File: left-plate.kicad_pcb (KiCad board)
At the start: 2 copper layers, 154.5 x 96.2 mm, 26 parts

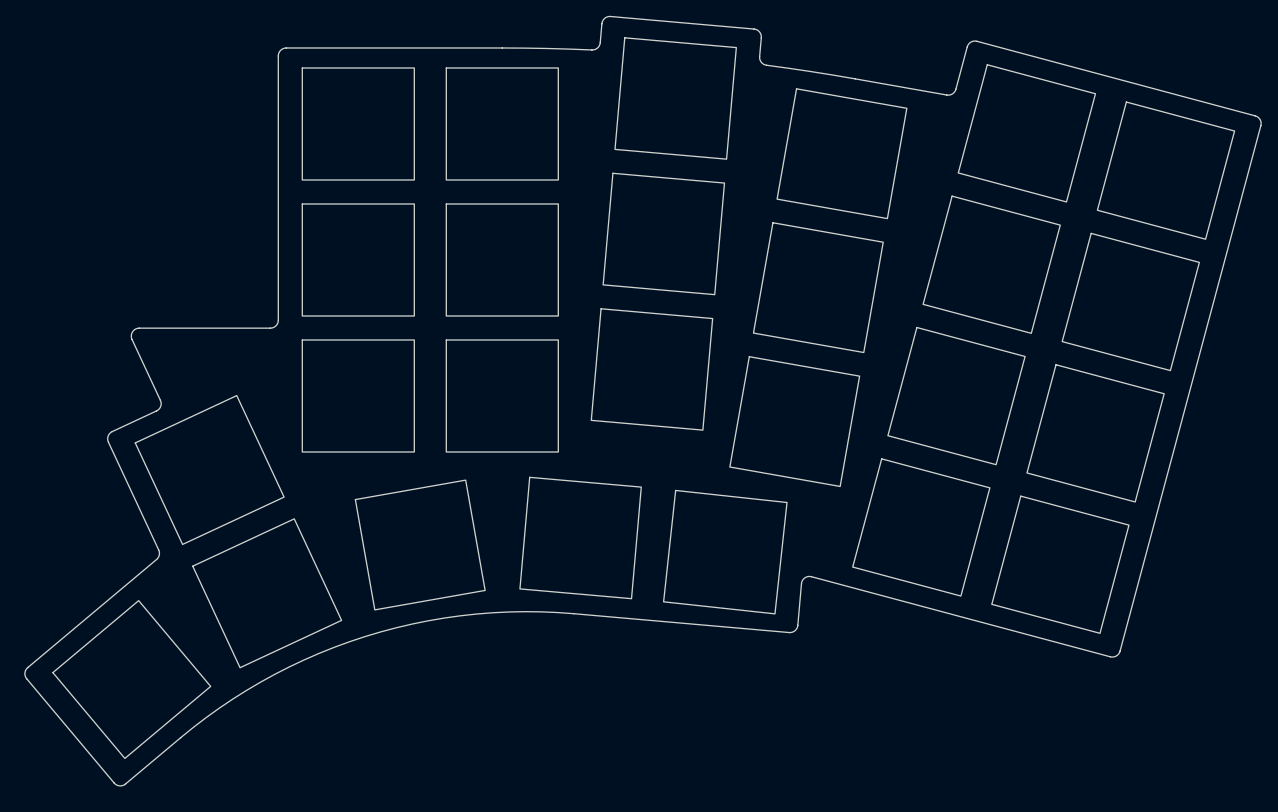
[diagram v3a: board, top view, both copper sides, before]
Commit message: remove two thumb keys
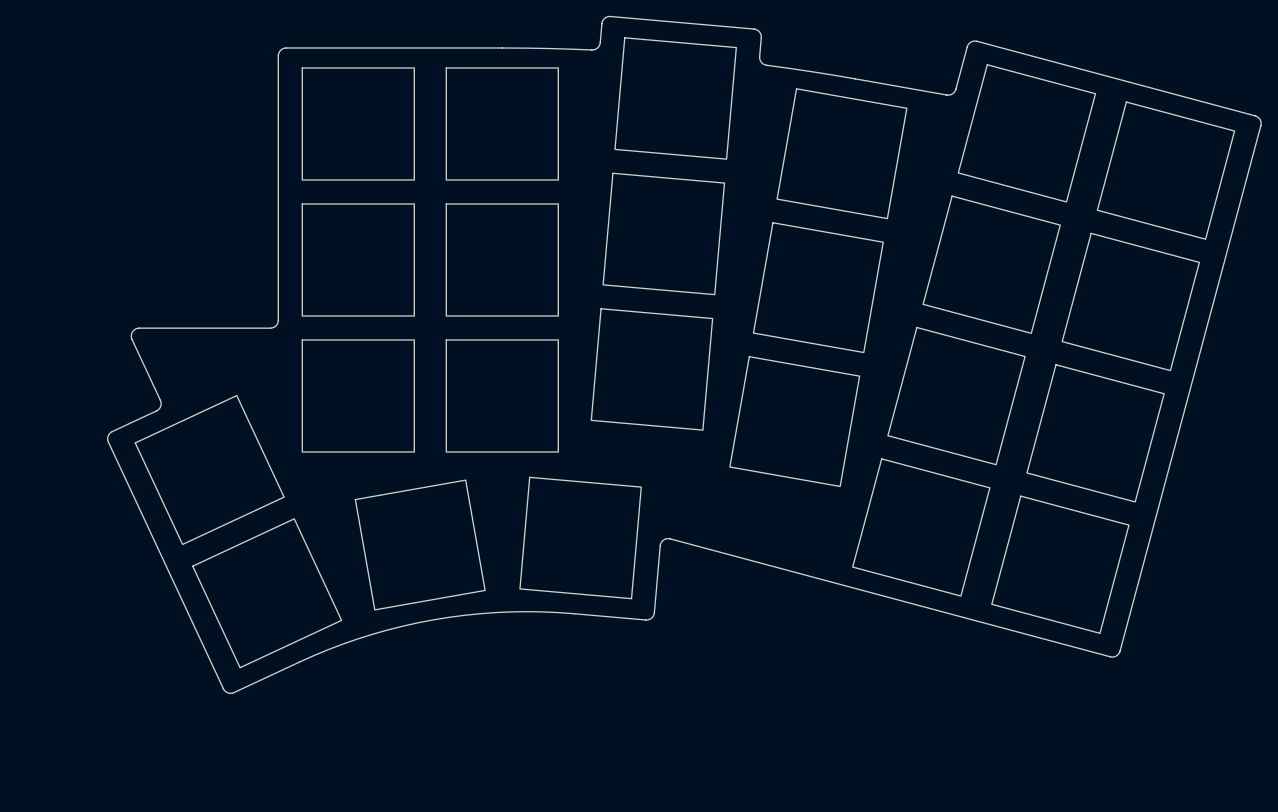
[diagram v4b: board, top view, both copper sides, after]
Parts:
- removed the REF** at (51.5, 128.9)
- removed the REF** at (125.7, 113.0)
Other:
- board size 154.5 x 96.2 mm -> 144.2 x 84.6 mm
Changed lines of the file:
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@@
-  )
-  (footprint "keyboard:KeyHole" (layer "F.Cu")
-    (at 125.654248 113.020897 -6.171)
-    (fp_text reference "REF**" (at 0 0 -6.171 unlocked) (layer "F.Fab") hide
-      (effects (font (size 1 1) (thickness 0.1)))
-    )
-    (fp_text value "KeyHole" (at 0 2 -6.171 unlocked) (layer "F.Fab") hide
-      (effects (font (size 1 1) (thickness 0.125)))
-    )
-    (fp_rect (start -7 -7) (end 7 7) (layer "Edge.Cuts") (stroke (width 0.12) (type default)) (fill none))
   )
   (footprint "keyboard:KeyHole" (layer "F.Cu")
@@
   )
   (footprint "keyboard:KeyHole" (layer "F.Cu")
-    (at 51.462952 128.941816 40)
-    (fp_text reference "REF**" (at 0 0 40 unlocked) (layer "F.Fab") hide
-      (effects (font (size 1 1) (thickness 0.1)))
-    )
-    (fp_text value "KeyHole" (at 0 2 40 unlocked) (layer "F.Fab") hide
-      (effects (font (size 1 1) (thickness 0.125)))
-    )
-    (fp_rect (start -7 -7) (end 7 7) (layer "Edge.Cuts") (stroke (width 0.12) (type default)) (fill none))
-  )
-  (footprint "keyboard:KeyHole" (layer "F.Cu")
     (at 79.78 59.5)
     (fp_text reference "REF**" (at 0 0 unlocked) (layer "F.Fab") hide
@@
     (fp_rect (start -7 -7) (end 7 7) (layer "Edge.Cuts") (stroke (width 0.12) (type default)) (fill none))
   )
-  (gr_arc (start 57.569435 136.219239) (mid 80.612677 123.577284) (end 106.739723 120.715907) (layer "Edge.Cuts") (width 0.12))
   (gr_arc (start 97.78 50) (mid 103.382237 50.061789) (end 108.981748 50.247127) (layer "Edge.Cuts") (width 0.12))
   (gr_arc (start 110.022044 49.335256) (mid 109.685013 50.000098) (end 108.981748 50.247126) (layer "Edge.Cuts") (width 0.12))
-  (gr_line (start 48.545718 99.276259) (end 54.828214 112.749115) (layer "Edge.Cuts") (width 0.12))
+  (gr_line (start 48.545718 99.276259) (end 62.914739 130.090724) (layer "Edge.Cuts") (width 0.12))
   (gr_line (start 69.78 51) (end 69.78 84.02) (layer "Edge.Cuts") (width 0.12))
   (gr_line (start 110.228748 46.972619) (end 110.022044 49.335256) (layer "Edge.Cuts") (width 0.12))
   (gr_arc (start 55.041575 94.040436) (mid 55.07496 94.805074) (end 54.557885 95.369362) (layer "Edge.Cuts") (width 0.12))
-  (gr_line (start 54.564694 113.937777) (end 38.46207 127.449483) (layer "Edge.Cuts") (width 0.12))
+  (gr_arc (start 117.519499 112.23964) (mid 117.942117 111.507643) (end 118.774513 111.36087) (layer "Edge.Cuts") (width 0.12))
   (gr_line (start 141.886567 53.858826) (end 153.339152 55.878225) (layer "Edge.Cuts") (width 0.12))
   (gr_arc (start 69.78 84.02) (mid 69.487107 84.727107) (end 68.78 85.02) (layer "Edge.Cuts") (width 0.12))
   (gr_arc (start 129.243603 47.632383) (mid 129.922491 47.98579) (end 130.152642 48.715734) (layer "Edge.Cuts") (width 0.12))
-  (gr_line (start 135.17438 116.970262) (end 134.720331 122.160072) (layer "Edge.Cuts") (width 0.12))
+  (gr_arc (start 116.788826 120.591269) (mid 116.435419 121.270158) (end 115.705476 121.500308) (layer "Edge.Cuts") (width 0.12))
   (gr_line (start 174.998839 125.390856) (end 192.598534 59.7079) (layer "Edge.Cuts") (width 0.12))
   (gr_line (start 54.557885 95.369362) (end 49.029408 97.947333) (layer "Edge.Cuts") (width 0.12))
-  (gr_line (start 173.774094 126.097963) (end 136.429395 116.091481) (layer "Edge.Cuts") (width 0.12))
-  (gr_arc (start 135.17438 116.970262) (mid 135.596995 116.238258) (end 136.429395 116.091481) (layer "Edge.Cuts") (width 0.12))
+  (gr_arc (start 64.243674 130.57441) (mid 63.479031 130.6078) (end 62.914739 130.090724) (layer "Edge.Cuts") (width 0.12))
+  (gr_line (start 173.774094 126.097963) (end 118.774513 111.36087) (layer "Edge.Cuts") (width 0.12))
+  (gr_line (start 64.243674 130.574409) (end 72.400435 126.770849) (layer "Edge.Cuts") (width 0.12))
   (gr_line (start 70.78 50) (end 97.78 50) (layer "Edge.Cuts") (width 0.12))
-  (gr_line (start 133.63698 123.069111) (end 106.739723 120.715906) (layer "Edge.Cuts") (width 0.12))
+  (gr_line (start 115.705476 121.500308) (end 106.739723 120.715906) (layer "Edge.Cuts") (width 0.12))
   (gr_line (start 191.891427 58.483155) (end 157.118097 49.16567) (layer "Edge.Cuts") (width 0.12))
   (gr_arc (start 174.998839 125.390856) (mid 174.532913 125.998062) (end 173.774094 126.097963) (layer "Edge.Cuts") (width 0.12))
   (gr_arc (start 110.228748 46.972619) (mid 110.582155 46.293731) (end 111.312099 46.06358) (layer "Edge.Cuts") (width 0.12))
   (gr_line (start 129.945938 51.07837) (end 130.152642 48.715734) (layer "Edge.Cuts") (width 0.12))
-  (gr_line (start 50.675035 142.004327) (end 57.569435 136.219239) (layer "Edge.Cuts") (width 0.12))
-  (gr_arc (start 50.675034 142.004326) (mid 49.945092 142.234476) (end 49.266203 141.88107) (layer "Edge.Cuts") (width 0.12))
   (gr_line (start 155.893352 49.872776) (end 154.478726 55.152236) (layer "Edge.Cuts") (width 0.12))
-  (gr_arc (start 54.828213 112.749115) (mid 54.898201 113.388172) (end 54.564693 113.937776) (layer "Edge.Cuts") (width 0.12))
-  (gr_line (start 49.266203 141.88107) (end 38.338813 128.858315) (layer "Edge.Cuts") (width 0.12))
+  (gr_line (start 117.519499 112.23964) (end 116.788826 120.591269) (layer "Edge.Cuts") (width 0.12))
   (gr_arc (start 130.812085 52.157035) (mid 130.162398 51.791639) (end 129.945937 51.07837) (layer "Edge.Cuts") (width 0.12))
   (gr_arc (start 48.545718 99.276259) (mid 48.512333 98.511621) (end 49.029408 97.947333) (layer "Edge.Cuts") (width 0.12))
@@
   (gr_line (start 55.041575 94.040436) (end 51.498654 86.442618) (layer "Edge.Cuts") (width 0.12))
   (gr_arc (start 130.812085 52.157035) (mid 136.358711 52.946858) (end 141.886567 53.858826) (layer "Edge.Cuts") (width 0.12))
-  (gr_arc (start 134.720331 122.160072) (mid 134.366924 122.838961) (end 133.63698 123.069112) (layer "Edge.Cuts") (width 0.12))
   (gr_line (start 52.404962 85.02) (end 68.78 85.02) (layer "Edge.Cuts") (width 0.12))
   (gr_arc (start 191.891427 58.483155) (mid 192.498633 58.949081) (end 192.598534 59.7079) (layer "Edge.Cuts") (width 0.12))
@@
   (gr_arc (start 155.893352 49.872776) (mid 156.359278 49.26557) (end 157.118097 49.16567) (layer "Edge.Cuts") (width 0.12))
   (gr_arc (start 154.478726 55.152236) (mid 154.050098 55.736805) (end 153.339152 55.878225) (layer "Edge.Cuts") (width 0.12))
-  (gr_arc (start 38.338814 128.858315) (mid 38.108663 128.128372) (end 38.46207 127.449483) (layer "Edge.Cuts") (width 0.12))
+  (gr_arc (start 72.400435 126.770849) (mid 89.171505 121.482954) (end 106.739723 120.715906) (layer "Edge.Cuts") (width 0.12))
 )

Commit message: remove area under palm
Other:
- outline, holes or cut-outs redrawn
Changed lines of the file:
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@@
   (gr_line (start 110.228748 46.972619) (end 110.022044 49.335256) (layer "Edge.Cuts") (width 0.12))
   (gr_arc (start 55.041575 94.040436) (mid 55.07496 94.805074) (end 54.557885 95.369362) (layer "Edge.Cuts") (width 0.12))
-  (gr_arc (start 117.519499 112.23964) (mid 117.942117 111.507643) (end 118.774513 111.36087) (layer "Edge.Cuts") (width 0.12))
+  (gr_arc (start 139.000764 116.780478) (mid 138.393558 116.314552) (end 138.293657 115.555733) (layer "Edge.Cuts") (width 0.12))
   (gr_line (start 141.886567 53.858826) (end 153.339152 55.878225) (layer "Edge.Cuts") (width 0.12))
   (gr_arc (start 69.78 84.02) (mid 69.487107 84.727107) (end 68.78 85.02) (layer "Edge.Cuts") (width 0.12))
@@
   (gr_line (start 54.557885 95.369362) (end 49.029408 97.947333) (layer "Edge.Cuts") (width 0.12))
   (gr_arc (start 64.243674 130.57441) (mid 63.479031 130.6078) (end 62.914739 130.090724) (layer "Edge.Cuts") (width 0.12))
-  (gr_line (start 173.774094 126.097963) (end 118.774513 111.36087) (layer "Edge.Cuts") (width 0.12))
+  (gr_line (start 173.774094 126.097963) (end 139.000764 116.780478) (layer "Edge.Cuts") (width 0.12))
+  (gr_arc (start 118.147883 105.05718) (mid 118.508889 104.371979) (end 119.250898 104.150059) (layer "Edge.Cuts") (width 0.12))
   (gr_line (start 64.243674 130.574409) (end 72.400435 126.770849) (layer "Edge.Cuts") (width 0.12))
   (gr_line (start 70.78 50) (end 97.78 50) (layer "Edge.Cuts") (width 0.12))
@@
   (gr_arc (start 110.228748 46.972619) (mid 110.582155 46.293731) (end 111.312099 46.06358) (layer "Edge.Cuts") (width 0.12))
   (gr_line (start 129.945938 51.07837) (end 130.152642 48.715734) (layer "Edge.Cuts") (width 0.12))
+  (gr_arc (start 119.250898 104.150057) (mid 125.98312 104.988487) (end 132.683213 106.053635) (layer "Edge.Cuts") (width 0.12))
   (gr_line (start 155.893352 49.872776) (end 154.478726 55.152236) (layer "Edge.Cuts") (width 0.12))
-  (gr_line (start 117.519499 112.23964) (end 116.788826 120.591269) (layer "Edge.Cuts") (width 0.12))
+  (gr_line (start 118.147883 105.05718) (end 116.788826 120.591269) (layer "Edge.Cuts") (width 0.12))
+  (gr_arc (start 139.397025 107.237461) (mid 140.066769 107.684969) (end 140.189303 108.481088) (layer "Edge.Cuts") (width 0.12))
   (gr_arc (start 130.812085 52.157035) (mid 130.162398 51.791639) (end 129.945937 51.07837) (layer "Edge.Cuts") (width 0.12))
   (gr_arc (start 48.545718 99.276259) (mid 48.512333 98.511621) (end 49.029408 97.947333) (layer "Edge.Cuts") (width 0.12))
@@
   (gr_line (start 52.404962 85.02) (end 68.78 85.02) (layer "Edge.Cuts") (width 0.12))
   (gr_arc (start 191.891427 58.483155) (mid 192.498633 58.949081) (end 192.598534 59.7079) (layer "Edge.Cuts") (width 0.12))
+  (gr_line (start 138.293657 115.555733) (end 140.189303 108.481088) (layer "Edge.Cuts") (width 0.12))
   (gr_arc (start 69.78 51) (mid 70.072893 50.292893) (end 70.78 50) (layer "Edge.Cuts") (width 0.12))
   (gr_line (start 129.243603 47.632384) (end 111.312099 46.06358) (layer "Edge.Cuts") (width 0.12))
   (gr_arc (start 155.893352 49.872776) (mid 156.359278 49.26557) (end 157.118097 49.16567) (layer "Edge.Cuts") (width 0.12))
   (gr_arc (start 154.478726 55.152236) (mid 154.050098 55.736805) (end 153.339152 55.878225) (layer "Edge.Cuts") (width 0.12))
+  (gr_line (start 139.397025 107.237462) (end 132.683213 106.053635) (layer "Edge.Cuts") (width 0.12))
   (gr_arc (start 72.400435 126.770849) (mid 89.171505 121.482954) (end 106.739723 120.715906) (layer "Edge.Cuts") (width 0.12))
 )
